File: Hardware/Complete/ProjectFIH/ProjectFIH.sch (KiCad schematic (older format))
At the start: 10 parts, among them J1 Conn_01x02_Male, U1 LM158

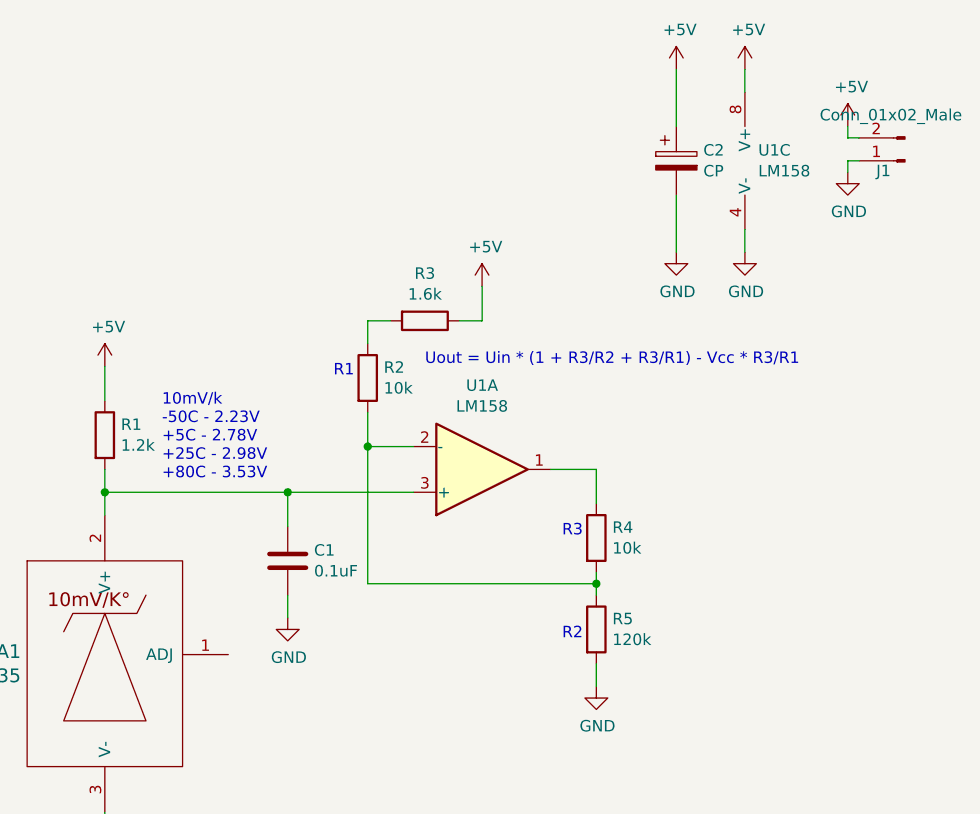
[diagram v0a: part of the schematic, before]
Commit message: Found that real LM358 saturates at 0.6V output (low). So, recalculated and retested.
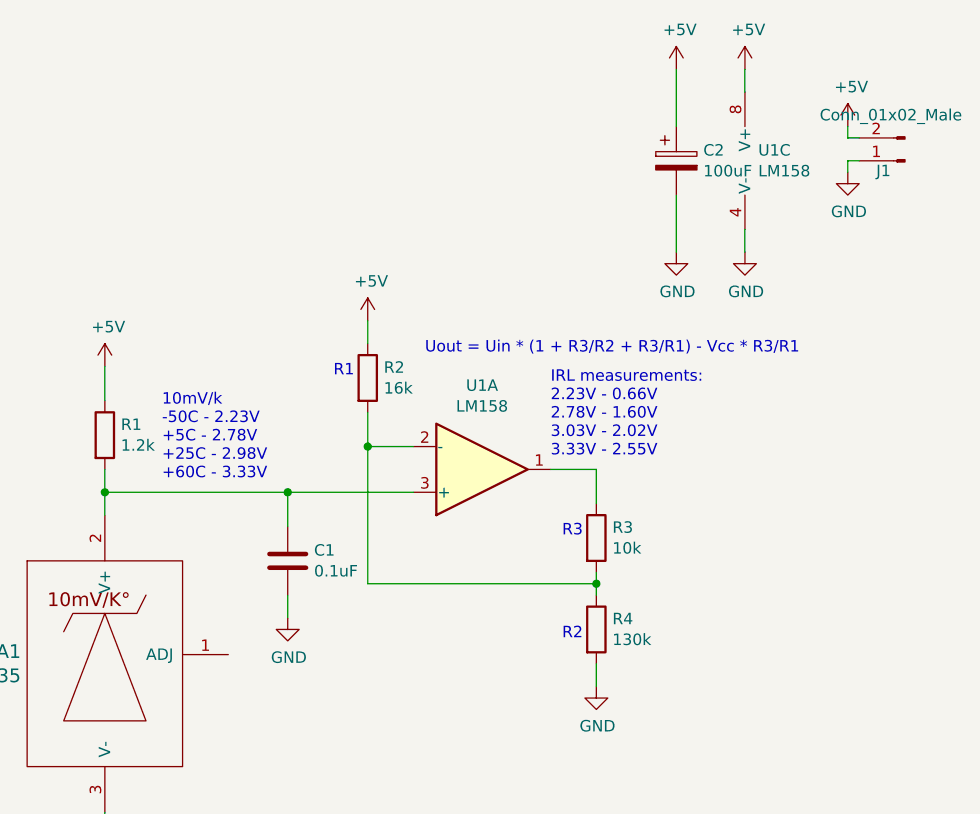
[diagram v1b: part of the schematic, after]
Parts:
- removed R3: 1.6k, symbol Device:R
- C2: value CP -> 100uF
- R2: value 10k -> 16k
- R4: renamed from R5; value 120k -> 130k
- renumbered R4 to R3
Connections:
- net +5V: now also R2.1
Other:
- note added: "10mV/k\n-50C - 2.23V\n+5C - 2.78V\n+25C - 2.98V\n+60C - 3.33V"
- note added: "IRL measurements:\n2.23V - 0.66V\n2.78V - 1.60V\n3.03V - 2.02V\n3.33V - 2.55V"
- note removed: "10mV/k\n-50C - 2.23V\n+5C - 2.78V\n+25C - 2.98V\n+80C - 3.53V"
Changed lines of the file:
@@
 P 2400 2100
 F 0 "R2" H 2470 2146 50  0000 L CNN
-F 1 "10k" H 2470 2055 50  0000 L CNN
+F 1 "16k" H 2470 2055 50  0000 L CNN
 F 2 "" V 2330 2100 50  0001 C CNN
 F 3 "~" H 2400 2100 50  0001 C CNN
@@
 $EndComp
 $Comp
-L Device:R R4
+L Device:R R3
 U 1 1 5EFCC8C6
 P 3400 2800
-F 0 "R4" H 3470 2846 50  0000 L CNN
+F 0 "R3" H 3470 2846 50  0000 L CNN
 F 1 "10k" H 3470 2755 50  0000 L CNN
 F 2 "" V 3330 2800 50  0001 C CNN
@@
 $EndComp
 $Comp
-L Device:R R5
+L Device:R R4
 U 1 1 5EFCCDFD
 P 3400 3200
-F 0 "R5" H 3470 3246 50  0000 L CNN
-F 1 "120k" H 3470 3155 50  0000 L CNN
+F 0 "R4" H 3470 3246 50  0000 L CNN
+F 1 "130k" H 3470 3155 50  0000 L CNN
 F 2 "" V 3330 3200 50  0001 C CNN
 F 3 "~" H 3400 3200 50  0001 C CNN
@@
 Wire Wire Line
 	3400 3000 3400 3050
-$Comp
-L Device:R R3
-U 1 1 5EFDCD05
-P 2650 1850
-F 0 "R3" V 2443 1850 50  0000 C CNN
-F 1 "1.6k" V 2534 1850 50  0000 C CNN
-F 2 "" V 2580 1850 50  0001 C CNN
-F 3 "~" H 2650 1850 50  0001 C CNN
-	1    2650 1850
-	0    1    1    0
-$EndComp
-Wire Wire Line
-	2500 1850 2400 1850
 Wire Wire Line
 	2400 1850 2400 1950
@@
 L power:+5V #PWR04
 U 1 1 5EFE0FC8
-P 2900 1700
-F 0 "#PWR04" H 2900 1550 50  0001 C CNN
-F 1 "+5V" H 2915 1873 50  0000 C CNN
-F 2 "" H 2900 1700 50  0001 C CNN
-F 3 "" H 2900 1700 50  0001 C CNN
-	1    2900 1700
+P 2400 1850
+F 0 "#PWR04" H 2400 1700 50  0001 C CNN
+F 1 "+5V" H 2415 2023 50  0000 C CNN
+F 2 "" H 2400 1850 50  0001 C CNN
+F 3 "" H 2400 1850 50  0001 C CNN
+	1    2400 1850
 	1    0    0    -1
 $EndComp
@@
 Wire Wire Line
 	4050 850  4050 750
-Wire Wire Line
-	2900 1700 2900 1850
-Wire Wire Line
-	2900 1850 2800 1850
 $Comp
 L Device:CP C2
@@
 P 3750 1150
 F 0 "C2" H 3868 1196 50  0000 L CNN
-F 1 "CP" H 3868 1105 50  0000 L CNN
+F 1 "100uF" H 3868 1105 50  0000 L CNN
 F 2 "" H 3788 1000 50  0001 C CNN
 F 3 "~" H 3750 1150 50  0001 C CNN
@@
 Wire Wire Line
 	4500 1150 4500 1200
-Text Notes 2650 2050 0    50   ~ 0
+Text Notes 2650 2000 0    50   ~ 0
 Uout = Uin * (1 + R3/R2 + R3/R1) - Vcc * R3/R1
 Text Notes 2250 2100 0    50   ~ 0
@@
 Connection ~ 2050 2600
 Text Notes 1500 2550 0    50   ~ 0
-10mV/k\n-50C - 2.23V\n+5C - 2.78V\n+25C - 2.98V\n+80C - 3.53V
+10mV/k\n-50C - 2.23V\n+5C - 2.78V\n+25C - 2.98V\n+60C - 3.33V
+Text Notes 3200 2450 0    50   ~ 0
+IRL measurements:\n2.23V - 0.66V\n2.78V - 1.60V\n3.03V - 2.02V\n3.33V - 2.55V
 $EndSCHEMATC

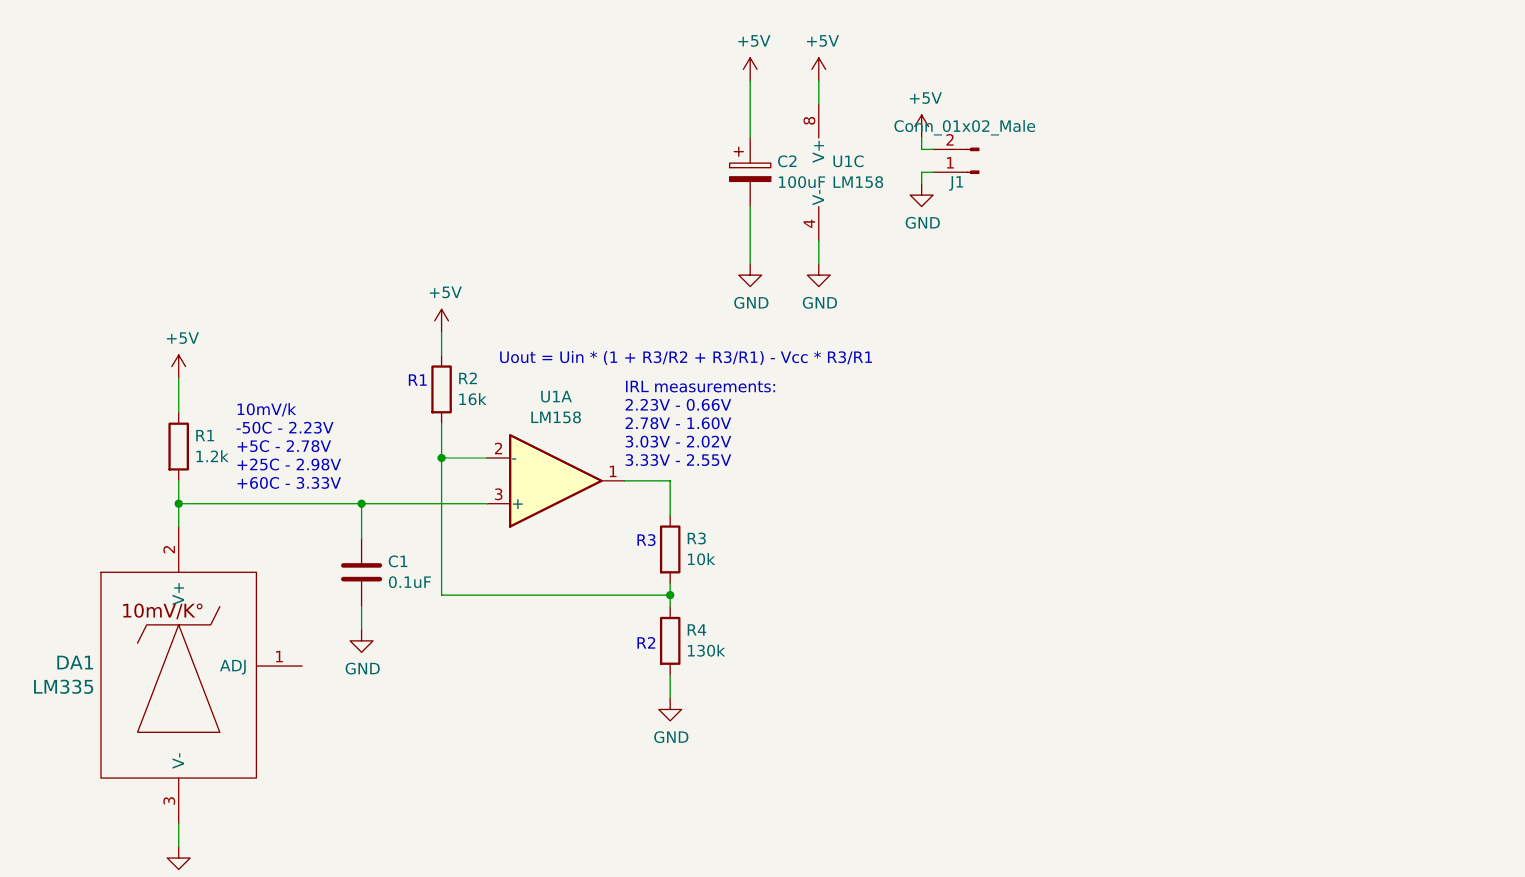
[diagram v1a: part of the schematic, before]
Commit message: Overheat protection comparator
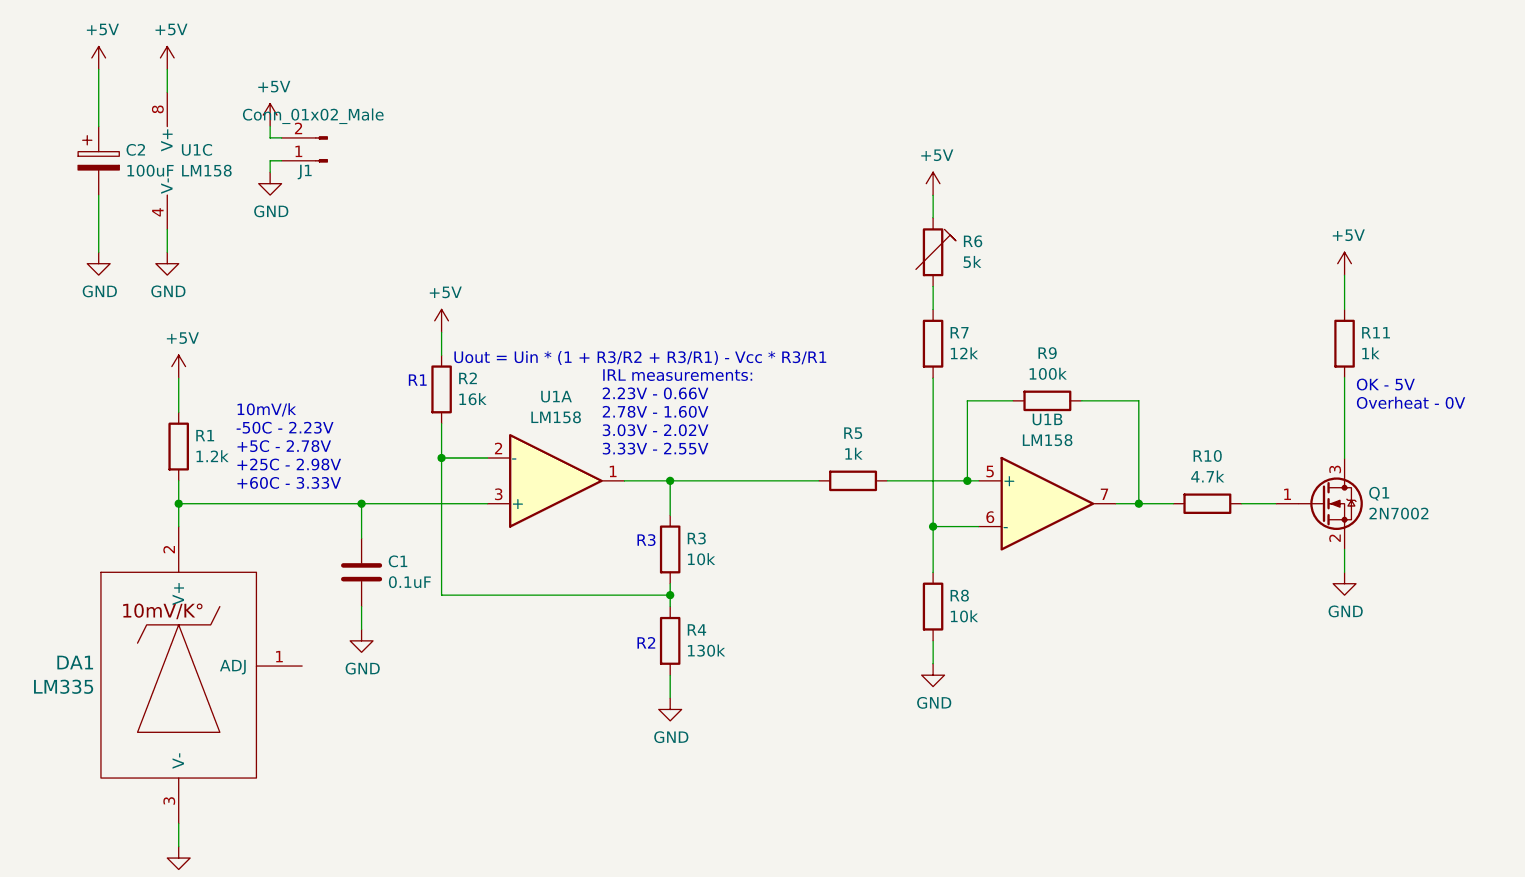
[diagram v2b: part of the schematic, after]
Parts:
- added Q1: 2N7002, Package_TO_SOT_SMD:SOT-23, symbol Transistor_FET:2N7002
- added R10: 4.7k, symbol Device:R
- added R11, R5: 1k, symbol Device:R
- added R6: 5k, symbol Device:RTRIM
- added R7: 12k, symbol Device:R
- added R8: 10k, symbol Device:R
- added R9: 100k, symbol Device:R
- added unit 2 of U1
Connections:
- net +5V: now also R11.1, R6.1
- net GND: now also Q1.2 (S), R8.2
- net at R3.1, U1.1: now also R5.2
- new net: R5.1, R9.2, U1.5 (+)
- new net: R7.2, R8.1, U1.6 (-)
- new net: R10.2, R9.1, U1.7
- new net: R6.2, R7.1
- new net: Q1.1 (G), R10.1
- new net: Q1.3 (D), R11.2
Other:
- note added: "OK - 5V\nOverheat - 0V"
- moved on the sheet: C2, J1, U1C

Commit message: Corrected hysterezis loop resistor.
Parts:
- R9: value 100k -> 75k
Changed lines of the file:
@@
 P 5050 2150
 F 0 "R9" V 4843 2150 50  0000 C CNN
-F 1 "100k" V 4934 2150 50  0000 C CNN
+F 1 "75k" V 4934 2150 50  0000 C CNN
 F 2 "" V 4980 2150 50  0001 C CNN
 F 3 "~" H 5050 2150 50  0001 C CNN

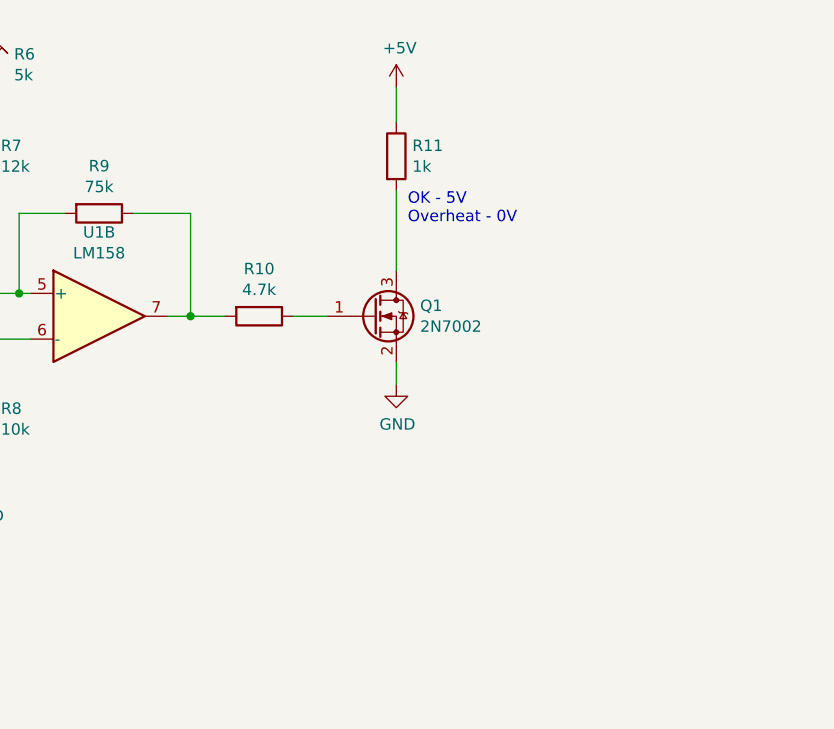
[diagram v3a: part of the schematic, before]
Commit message: Output stage, heat control.
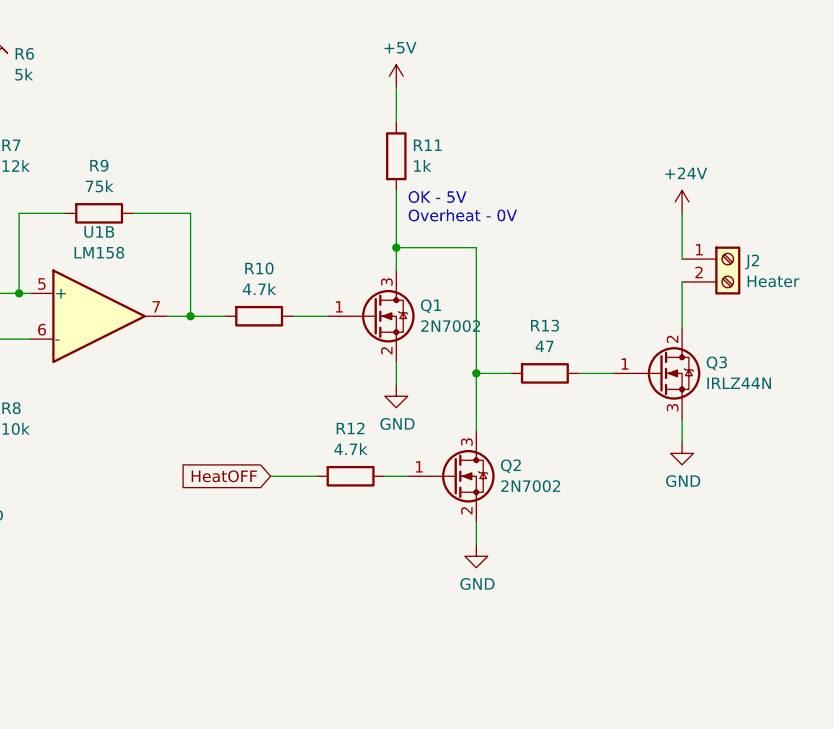
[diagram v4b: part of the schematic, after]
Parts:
- added J2: Heater, symbol Connector:Screw_Terminal_01x02
- added Q2: 2N7002, Package_TO_SOT_SMD:SOT-23, symbol Transistor_FET:2N7002
- added Q3: IRLZ44N, Package_TO_SOT_THT:TO-220-3_Vertical, symbol Transistor_FET:IRLZ44N
- added R12: 4.7k, symbol Device:R
- added R13: 47, symbol Device:R
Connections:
- net GND: now also Q2.2 (S), Q3.3 (S)
- net at Q1.3 (D), R11.2: now also Q2.3 (D), R13.2
- new net: Q2.1 (G), R12.1
- new net: Q3.1 (G), R13.1
- new net: J2.2 (Pin_2), Q3.2 (D)
- new net +24V: J2.1 (Pin_1)
- new net HeatOFF: R12.2
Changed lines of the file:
@@
 	6350 2800 6350 2900
 Wire Wire Line
-	6350 2400 6350 2050
+	6350 2400 6350 2300
 $Comp
 L power:+5V #PWR014
@@
 Text Notes 6400 2200 0    50   ~ 0
 OK - 5V\nOverheat - 0V
+$Comp
+L Transistor_FET:2N7002 Q2
+U 1 1 5F010FE4
+P 6600 3300
+F 0 "Q2" H 6804 3346 50  0000 L CNN
+F 1 "2N7002" H 6804 3255 50  0000 L CNN
+F 2 "Package_TO_SOT_SMD:SOT-23" H 6800 3225 50  0001 L CIN
+F 3 "https://www.fairchildsemi.com/datasheets/2N/2N7002.pdf" H 6600 3300 50  0001 L CNN
+	1    6600 3300
+	1    0    0    -1
+$EndComp
+$Comp
+L power:GND #PWR016
+U 1 1 5F014E6F
+P 6700 3600
+F 0 "#PWR016" H 6700 3350 50  0001 C CNN
+F 1 "GND" H 6705 3427 50  0000 C CNN
+F 2 "" H 6700 3600 50  0001 C CNN
+F 3 "" H 6700 3600 50  0001 C CNN
+	1    6700 3600
+	1    0    0    -1
+$EndComp
+Wire Wire Line
+	6700 3500 6700 3600
+Wire Wire Line
+	6700 3100 6700 2850
+Wire Wire Line
+	6700 2300 6350 2300
+Connection ~ 6350 2300
+Wire Wire Line
+	6350 2300 6350 2050
+Text GLabel 5800 3300 0    50   Input ~ 0
+HeatOFF
+$Comp
+L Device:R R12
+U 1 1 5F018879
+P 6150 3300
+F 0 "R12" V 5943 3300 50  0000 C CNN
+F 1 "4.7k" V 6034 3300 50  0000 C CNN
+F 2 "" V 6080 3300 50  0001 C CNN
+F 3 "~" H 6150 3300 50  0001 C CNN
+	1    6150 3300
+	0    1    1    0
+$EndComp
+Wire Wire Line
+	6400 3300 6300 3300
+Wire Wire Line
+	6000 3300 5800 3300
+$Comp
+L Device:R R13
+U 1 1 5F0296C2
+P 7000 2850
+F 0 "R13" V 6793 2850 50  0000 C CNN
+F 1 "47" V 6884 2850 50  0000 C CNN
+F 2 "" V 6930 2850 50  0001 C CNN
+F 3 "~" H 7000 2850 50  0001 C CNN
+	1    7000 2850
+	0    1    1    0
+$EndComp
+Wire Wire Line
+	6850 2850 6700 2850
+Connection ~ 6700 2850
+Wire Wire Line
+	6700 2850 6700 2300
+$Comp
+L Transistor_FET:IRLZ44N Q3
+U 1 1 5F02FAAF
+P 7500 2850
+F 0 "Q3" H 7704 2896 50  0000 L CNN
+F 1 "IRLZ44N" H 7704 2805 50  0000 L CNN
+F 2 "Package_TO_SOT_THT:TO-220-3_Vertical" H 7750 2775 50  0001 L CIN
+F 3 "http://www.irf.com/product-info/datasheets/data/irlz44n.pdf" H 7500 2850 50  0001 L CNN
+	1    7500 2850
+	1    0    0    -1
+$EndComp
+Wire Wire Line
+	7300 2850 7150 2850
+$Comp
+L power:GND #PWR018
+U 1 1 5F031AC1
+P 7600 3150
+F 0 "#PWR018" H 7600 2900 50  0001 C CNN
+F 1 "GND" H 7605 2977 50  0000 C CNN
+F 2 "" H 7600 3150 50  0001 C CNN
+F 3 "" H 7600 3150 50  0001 C CNN
+	1    7600 3150
+	1    0    0    -1
+$EndComp
+Wire Wire Line
+	7600 3050 7600 3150
+$Comp
+L Connector:Screw_Terminal_01x02 J2
+U 1 1 5F039ABC
+P 7800 2350
+F 0 "J2" H 7880 2342 50  0000 L CNN
+F 1 "Heater" H 7880 2251 50  0000 L CNN
+F 2 "" H 7800 2350 50  0001 C CNN
+F 3 "~" H 7800 2350 50  0001 C CNN
+	1    7800 2350
+	1    0    0    -1
+$EndComp
+Wire Wire Line
+	7600 2450 7600 2650
+$Comp
+L power:+24V #PWR017
+U 1 1 5F03C9B5
+P 7600 2150
+F 0 "#PWR017" H 7600 2000 50  0001 C CNN
+F 1 "+24V" H 7615 2323 50  0000 C CNN
+F 2 "" H 7600 2150 50  0001 C CNN
+F 3 "" H 7600 2150 50  0001 C CNN
+	1    7600 2150
+	1    0    0    -1
+$EndComp
+Wire Wire Line
+	7600 2150 7600 2350
 $EndSCHEMATC
